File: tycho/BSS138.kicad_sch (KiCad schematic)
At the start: 2 parts

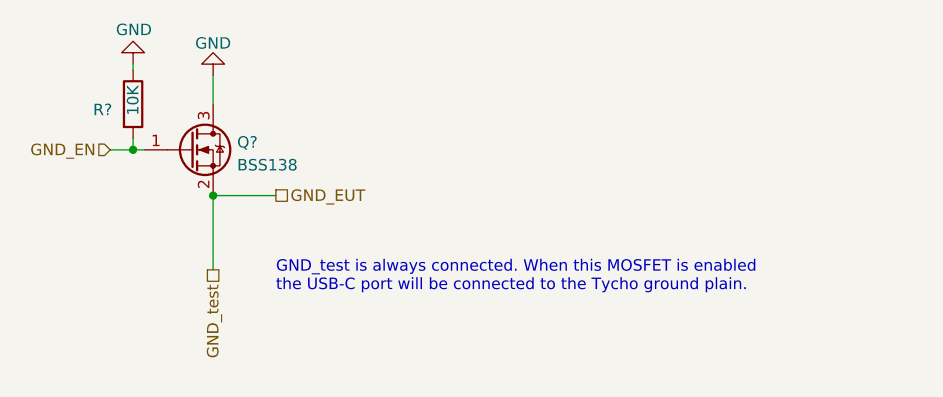
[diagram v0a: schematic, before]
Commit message: Tycho Hardware: Fix broken sheet link.
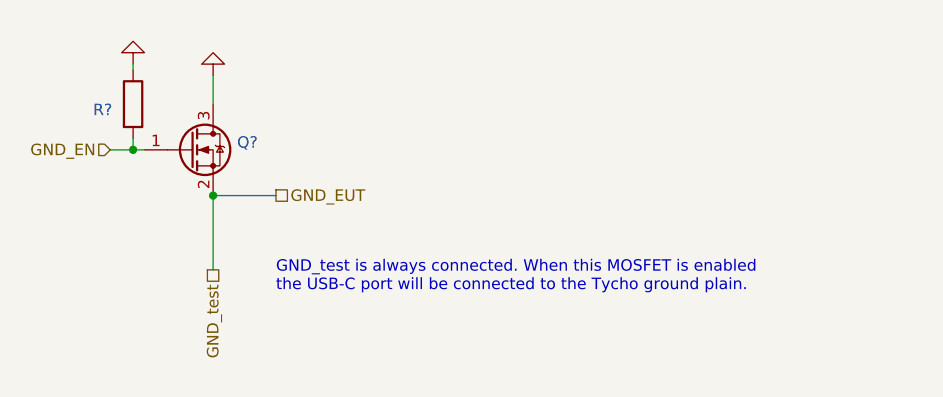
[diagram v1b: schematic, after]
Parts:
- Q?: value BSS138 -> (none); footprint Package_TO_SOT_SMD:SOT-23 -> (none)
- R?: value 10K -> (none); footprint Resistor_SMD:R_0603_1608Metric_Pad0.98x0.95mm_HandSolder -> (none)
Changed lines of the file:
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@@
       (effects (font (size 1.27 1.27)) hide)
     )
-    (property "Value" "GND" (id 1) (at 145.415 57.15 0)
+    (property "Value" "" (id 1) (at 145.415 57.15 0)
       (effects (font (size 1.27 1.27)) (justify right))
     )
@@
       (effects (font (size 1.27 1.27)) (justify left))
     )
-    (property "Value" "10K" (id 1) (at 147.32 66.675 90)
+    (property "Value" "" (id 1) (at 147.32 66.675 90)
       (effects (font (size 1.27 1.27)) (justify left))
     )
-    (property "Footprint" "Resistor_SMD:R_0603_1608Metric_Pad0.98x0.95mm_HandSolder" (id 2) (at 145.542 65.405 90)
+    (property "Footprint" "" (id 2) (at 145.542 65.405 90)
       (effects (font (size 1.27 1.27)) hide)
     )
@@
       (effects (font (size 1.27 1.27)) hide)
     )
-    (property "Value" "GND" (id 1) (at 156.21 58.6542 0))
+    (property "Value" "" (id 1) (at 156.21 58.6542 0))
     (property "Footprint" "" (id 2) (at 156.21 62.23 0)
       (effects (font (size 1.27 1.27)) hide)
@@
       (effects (font (size 1.27 1.27)) (justify left))
     )
-    (property "Value" "BSS138" (id 1) (at 158.877 72.1872 0)
+    (property "Value" "" (id 1) (at 158.877 72.1872 0)
       (effects (font (size 1.27 1.27)) (justify left))
     )
-    (property "Footprint" "Package_TO_SOT_SMD:SOT-23" (id 2) (at 158.75 72.39 0)
+    (property "Footprint" "" (id 2) (at 158.75 72.39 0)
       (effects (font (size 1.27 1.27) italic) (justify left) hide)
     )
